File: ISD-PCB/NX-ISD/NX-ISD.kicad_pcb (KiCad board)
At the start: 4 copper layers, 77 x 45 mm, 79 parts, among them J1 1-2328702-0, P1 S2B-PH-SM4-TB, Q1 AO3400A, Q2 AO3401A, Q3 BC847W, Q4 AO3400A, U1 ESP32-S3-WROOM-1, U10 BNO085, U11 HYCW275-USBC24-050B, U12 OPT3001DNPR, U13 RT9193-18GB, U14 ZDSD02GLGEAG, U15 USBLC6-2P6, U2 NCP167BMX330TBG, U3 MAX17048G_T10, U4 RV-3028-C7, U5 MAX30102, U6 BME690, U7 TM-2025A, U8 BQ25170DSGR, U9 RT9193-28GB, Y2 32.768

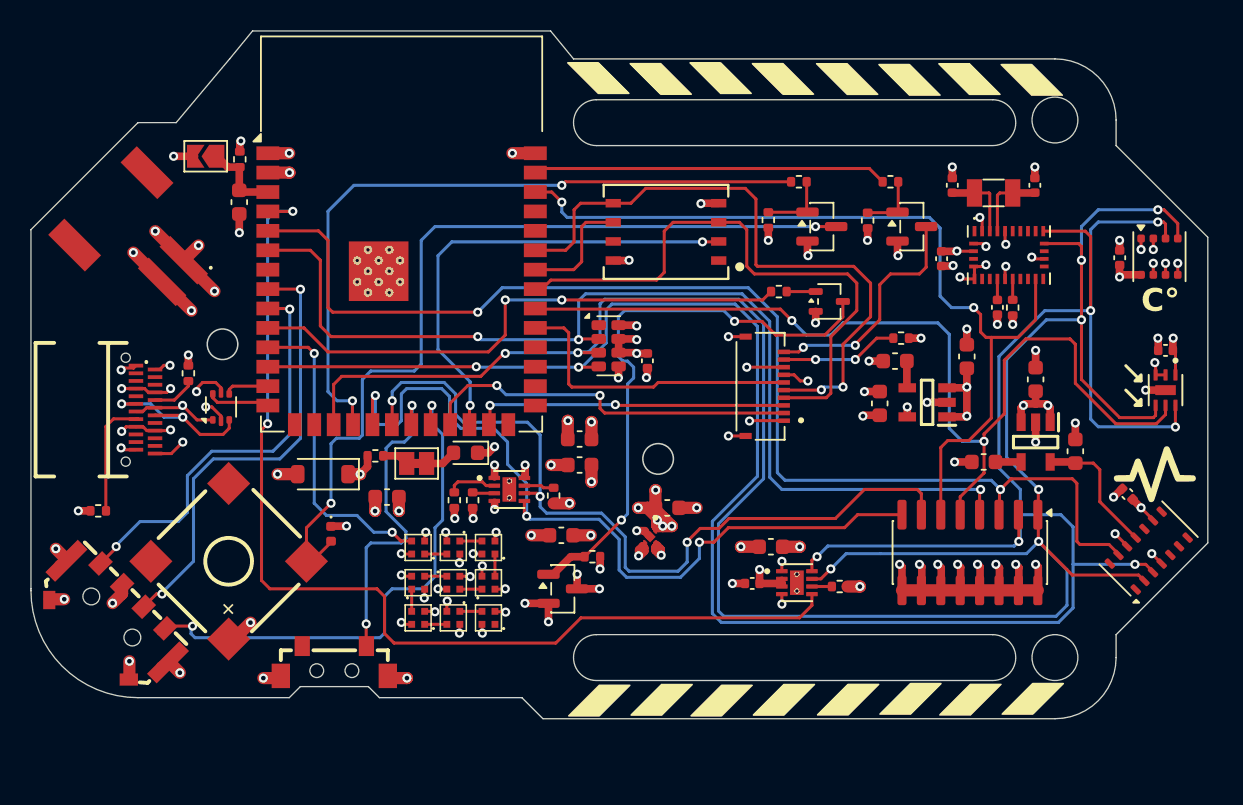
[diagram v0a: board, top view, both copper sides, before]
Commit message: Updated v1p0 files
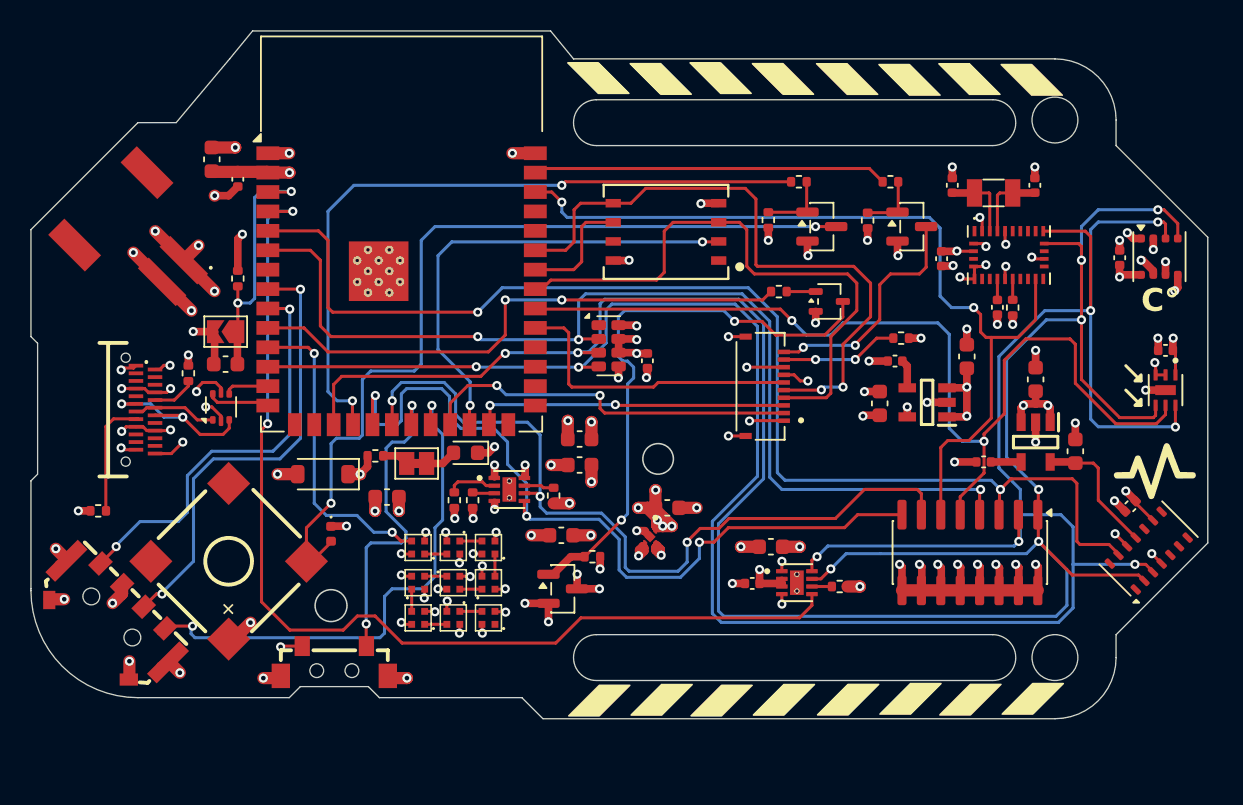
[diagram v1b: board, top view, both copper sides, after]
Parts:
- added C16: 10u, Capacitor_SMD:C_0603_1608Metric, F.Cu at (124.2, 86.5)
- added C17: 100n, Capacitor_SMD:C_0402_1005Metric, F.Cu at (125.9, 87.8)
- C11, C14: footprint Capacitor_SMD:C_0603_1608Metric -> Capacitor_SMD:C_0402_1005Metric
- C20, C21, C8: value 1uF -> 1u
- C22: value 10uF -> 10u
- S1: value TS18-5-15-SL-260 -> TS-1101VS-C-A-A
- moved JP2 11.5 mm to (125.1, 97.8)
- moved C8 10.6 mm to (125.1, 99.9), turned to 180 degrees
- moved R3 7.80 mm to (125.9, 94.3)
- moved C5 0.82 mm to (184.3, 109.2), turned to -135 degrees
- moved G*** 0.20 mm to (187.4, 106.9)
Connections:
- S1 pad 2: unconnected-(S1-Pad2) -> GND
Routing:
- net /Logic section/EN: track 5.25 -> 17.2 mm, vias 0 -> 2
- net GND: track 90.3 -> 97.5 mm, vias 86 -> 88
- net +3V3: track 63.1 -> 69.5 mm
- net /Power section/U_D+: track 5.78 -> 5.46 mm, vias 1 -> 0
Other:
- outline, holes or cut-outs redrawn
- board text added: "LED"
- board text added: "P: IO17 D: IO18"
- board text removed: "CHRG LED"
- board text removed: "POWER: IO17 DATA: IO18"

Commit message: updated label
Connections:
- net /Logic section/!INT_H renamed /Logic section/!INT_DOF
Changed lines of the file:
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@@
 			(layers "F.Cu" "F.Mask" "F.Paste")
 			(roundrect_rratio 0.25)
-			(net "/Logic section/!INT_H")
+			(net "/Logic section/!INT_DOF")
 			(pinfunction "R6.1_6")
 			(pintype "passive")
@@
 			(size 0.25 0.675)
 			(layers "F.Cu" "F.Mask" "F.Paste")
-			(net "/Logic section/!INT_H")
+			(net "/Logic section/!INT_DOF")
 			(pinfunction "~{H_INT}_14")
 			(pintype "output")
@@
 			(size 1.5 0.9)
 			(layers "F.Cu" "F.Mask" "F.Paste")
-			(net "/Logic section/!INT_H")
+			(net "/Logic section/!INT_DOF")
 			(pinfunction "IO2_38")
 			(pintype "bidirectional")
@@
 		(width 0.2)
 		(layer "F.Cu")
-		(net "/Logic section/!INT_H")
+		(net "/Logic section/!INT_DOF")
 	)
 	(segment
@@
 		(width 0.2)
 		(layer "F.Cu")
-		(net "/Logic section/!INT_H")
+		(net "/Logic section/!INT_DOF")
 	)
 	(segment
@@
 		(width 0.2)
 		(layer "F.Cu")
-		(net "/Logic section/!INT_H")
+		(net "/Logic section/!INT_DOF")
 	)
 	(segment
@@
 		(width 0.2)
 		(layer "F.Cu")
-		(net "/Logic section/!INT_H")
+		(net "/Logic section/!INT_DOF")
 	)
 	(segment
@@
 		(width 0.2)
 		(layer "F.Cu")
-		(net "/Logic section/!INT_H")
+		(net "/Logic section/!INT_DOF")
 	)
 	(segment
@@
 		(width 0.2)
 		(layer "F.Cu")
-		(net "/Logic section/!INT_H")
+		(net "/Logic section/!INT_DOF")
 	)
 	(segment
@@
 		(width 0.2)
 		(layer "F.Cu")
-		(net "/Logic section/!INT_H")
+		(net "/Logic section/!INT_DOF")
 	)
 	(segment
@@
 		(width 0.2)
 		(layer "F.Cu")
-		(net "/Logic section/!INT_H")
+		(net "/Logic section/!INT_DOF")
 	)
 	(segment
@@
 		(width 0.2)
 		(layer "F.Cu")
-		(net "/Logic section/!INT_H")
+		(net "/Logic section/!INT_DOF")
 	)
 	(segment
@@
 		(width 0.2)
 		(layer "F.Cu")
-		(net "/Logic section/!INT_H")
+		(net "/Logic section/!INT_DOF")
 	)
 	(segment
@@
 		(width 0.2)
 		(layer "F.Cu")
-		(net "/Logic section/!INT_H")
+		(net "/Logic section/!INT_DOF")
 	)
 	(segment
@@
 		(width 0.2)
 		(layer "F.Cu")
-		(net "/Logic section/!INT_H")
+		(net "/Logic section/!INT_DOF")
 	)
 	(segment
@@
 		(width 0.2)
 		(layer "F.Cu")
-		(net "/Logic section/!INT_H")
+		(net "/Logic section/!INT_DOF")
 	)
 	(segment
@@
 		(width 0.2)
 		(layer "F.Cu")
-		(net "/Logic section/!INT_H")
+		(net "/Logic section/!INT_DOF")
 	)
 	(via
@@
 		(drill 0.3)
 		(layers "F.Cu" "B.Cu")
-		(net "/Logic section/!INT_H")
+		(net "/Logic section/!INT_DOF")
 	)
 	(via
@@
 		(drill 0.3)
 		(layers "F.Cu" "B.Cu")
-		(net "/Logic section/!INT_H")
+		(net "/Logic section/!INT_DOF")
 	)
 	(segment
@@
 		(width 0.2)
 		(layer "B.Cu")
-		(net "/Logic section/!INT_H")
+		(net "/Logic section/!INT_DOF")
 	)
 	(segment
@@
 		(width 0.2)
 		(layer "B.Cu")
-		(net "/Logic section/!INT_H")
+		(net "/Logic section/!INT_DOF")
 	)
 	(segment
@@
 		(width 0.2)
 		(layer "B.Cu")
-		(net "/Logic section/!INT_H")
+		(net "/Logic section/!INT_DOF")
 	)
 	(segment
@@
 		(width 0.2)
 		(layer "B.Cu")
-		(net "/Logic section/!INT_H")
+		(net "/Logic section/!INT_DOF")
 	)
 	(segment
@@
 		(width 0.2)
 		(layer "B.Cu")
-		(net "/Logic section/!INT_H")
+		(net "/Logic section/!INT_DOF")
 	)
 	(segment
@@
 		(width 0.2)
 		(layer "B.Cu")
-		(net "/Logic section/!INT_H")
+		(net "/Logic section/!INT_DOF")
 	)
 	(segment
@@
 		(width 0.2)
 		(layer "B.Cu")
-		(net "/Logic section/!INT_H")
+		(net "/Logic section/!INT_DOF")
 	)
 	(segment

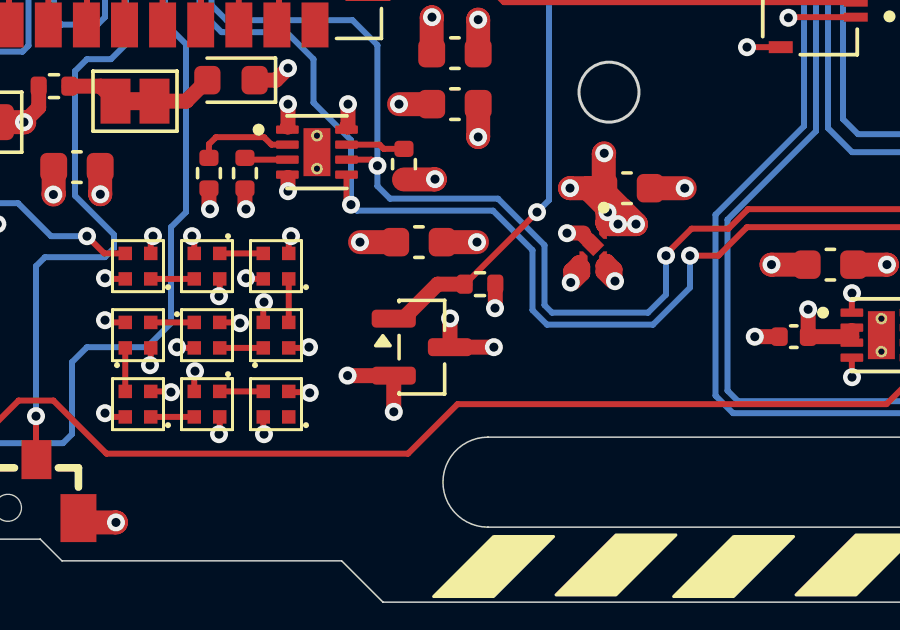
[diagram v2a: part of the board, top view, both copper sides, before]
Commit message: Fixed: polarity of NPM Pmos
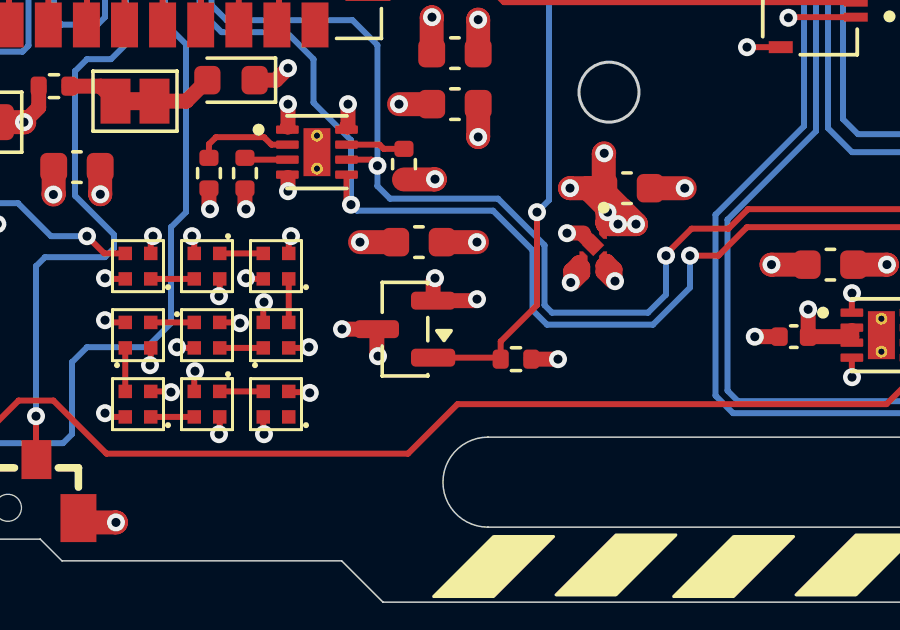
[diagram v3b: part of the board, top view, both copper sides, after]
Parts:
- moved R12 2.77 mm to (150.3, 115.0)
- moved Q2 0.82 mm to (146.6, 114.0), turned to 180 degrees
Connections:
- net /Logic section/!INT_DOF renamed /Logic section/!INT_H
- Q2 pad 2: VN -> VBAT
- Q2 pad 3: VBAT -> VN
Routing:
- net Net-(Q2-G): track 37.5 -> 38.9 mm
- net VN: track 8.44 -> 7.77 mm
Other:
- board text added: "v1p1"
- board text removed: "v1p0"

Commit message: v1p1 rework in progress
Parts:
- added C18: 100n, Capacitor_SMD:C_0402_1005Metric, F.Cu at (182.8, 112.1)
- added G10: XL-1010RGBC-WS2812B, NX-AW-footprints:LED-SMD_4P-L1.0-W1.0-TL_XL-1010RGBC-WS2812B, F.Cu at (139.6, 117.0)
- added G11: XL-1010RGBC-WS2812B, NX-AW-footprints:LED-SMD_4P-L1.0-W1.0-TL_XL-1010RGBC-WS2812B, F.Cu at (141.9, 117.0)
- added G12: XL-1010RGBC-WS2812B, NX-AW-footprints:LED-SMD_4P-L1.0-W1.0-TL_XL-1010RGBC-WS2812B, F.Cu at (144.1, 117.0)
- added G13: XL-1010RGBC-WS2812B, NX-AW-footprints:LED-SMD_4P-L1.0-W1.0-TL_XL-1010RGBC-WS2812B, F.Cu at (144.1, 119.3)
- added G14: XL-1010RGBC-WS2812B, NX-AW-footprints:LED-SMD_4P-L1.0-W1.0-TL_XL-1010RGBC-WS2812B, F.Cu at (141.9, 119.3)
- added G15: XL-1010RGBC-WS2812B, NX-AW-footprints:LED-SMD_4P-L1.0-W1.0-TL_XL-1010RGBC-WS2812B, F.Cu at (139.6, 119.3)
- added G16: XL-1010RGBC-WS2812B, NX-AW-footprints:LED-SMD_4P-L1.0-W1.0-TL_XL-1010RGBC-WS2812B, F.Cu at (137.2, 119.3)
- added JP3: BOOT, Jumper:SolderJumper-2_P1.3mm_Open_TrianglePad1.0x1.5mm, B.Cu at (135.8, 99.0)
- added R18: 10k, Resistor_SMD:R_0402_1005Metric, F.Cu at (171.5, 93.7)
- added R19: 10k, Resistor_SMD:R_0402_1005Metric, F.Cu at (180.1, 93.2)
- J1: footprint Global Footprints:TE_1-2328702-0 -> NX-AW-footprints:TE_1-2328702-0
- U14: footprint Global Footprints:LGA-8_L8.0-W6.0-P1.27-TL_ZDSD02GLGEAG -> NX-AW-footprints:LGA-8_L8.0-W6.0-P1.27-TL_ZDSD02GLGEAG
- moved G9 5.13 mm to (137.2, 117.1)
- moved R15 4.83 mm to (165.4, 101.0)
- moved G6 4.21 mm to (141.9, 114.8), turned to 0 degrees
- moved G5 4.14 mm to (144.1, 114.8), turned to 90 degrees
- moved R14 4.10 mm to (170.3, 88.0), turned to 0 degrees
- moved G8 3.23 mm to (137.3, 114.8), turned to 90 degrees
- moved G7 2.55 mm to (139.6, 114.8), turned to 90 degrees
- moved G4 2.49 mm to (144.1, 112.5), turned to 180 degrees
- moved S1 2.24 mm to (132.2, 121.6)
- moved U7 2.20 mm to (117.6, 118.7)
- moved RN1 2.06 mm to (173.8, 114.3)
- moved J1 1.91 mm to (162.9, 105.0)
- moved C1 1.51 mm to (183.4, 94.4)
- moved C12 1.51 mm to (186.4, 100.5)
- moved G*** 1.51 mm to (187.3, 108.4)
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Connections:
- net /Logic section/RS renamed /Logic section/DC
- net /Sernsor section/SCL_1 renamed /Logic section/SCL_1
- net /Sernsor section/SDA_1 renamed /Logic section/SDA_1
- G9 pad 1: unconnected-(G9-DOUT-Pad1) -> Net-(G10-DIN)
- U1 pad 27: unconnected-(U1-IO0-Pad27) -> /Logic section/BOOT
- U10 pad 18: unconnected-(U10-~{H_CS}-Pad18) -> Net-(U10-~{H_CS})
- U10 pad 4: unconnected-(U10-~{BOOT}-Pad4) -> Net-(U10-~{BOOT})
- U3 pad 10: GND -> (no net)
- U3 pad 11: GND -> (no net)
- U8 pad 10: GND -> (no net)
- U8 pad 11: GND -> (no net)
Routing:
- net /Logic section/SCL_1: track 155.4 -> 128.7 mm, vias 8 -> 7
- net /Logic section/SDA_1: track 166.2 -> 147.0 mm
- net /Logic section/!ALERT: track 68.4 -> 87.4 mm, vias 2 -> 3
- net GND: track 97.5 -> 80.0 mm, vias 88 -> 74
- net Net-(Q4-D): track 15.7 -> 0.00 mm, vias 2 -> 0
- net /Logic section/CS_TFT: track 20.8 -> 9.86 mm
- net /Logic section/BOOT: track 0.00 -> 10.3 mm, vias 0 -> 1
- net /Logic section/MOSI: track 41.4 -> 32.1 mm, vias 2 -> 0
- net /Logic section/SCK: track 38.6 -> 29.3 mm
- net /Logic section/!INT_HR: track 78.8 -> 70.5 mm
- net /Logic section/RST: track 19.9 -> 11.7 mm
- net Net-(J1-Pad9): track 7.82 -> 0.00 mm, vias 2 -> 0
- net +1V8: track 8.92 -> 3.33 mm
- net VN: track 7.77 -> 2.57 mm, vias 11 -> 3
- net /Logic section/LEVER_LEFT: track 34.5 -> 29.3 mm
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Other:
- board size 77 x 45 mm -> 77 x 48.6 mm

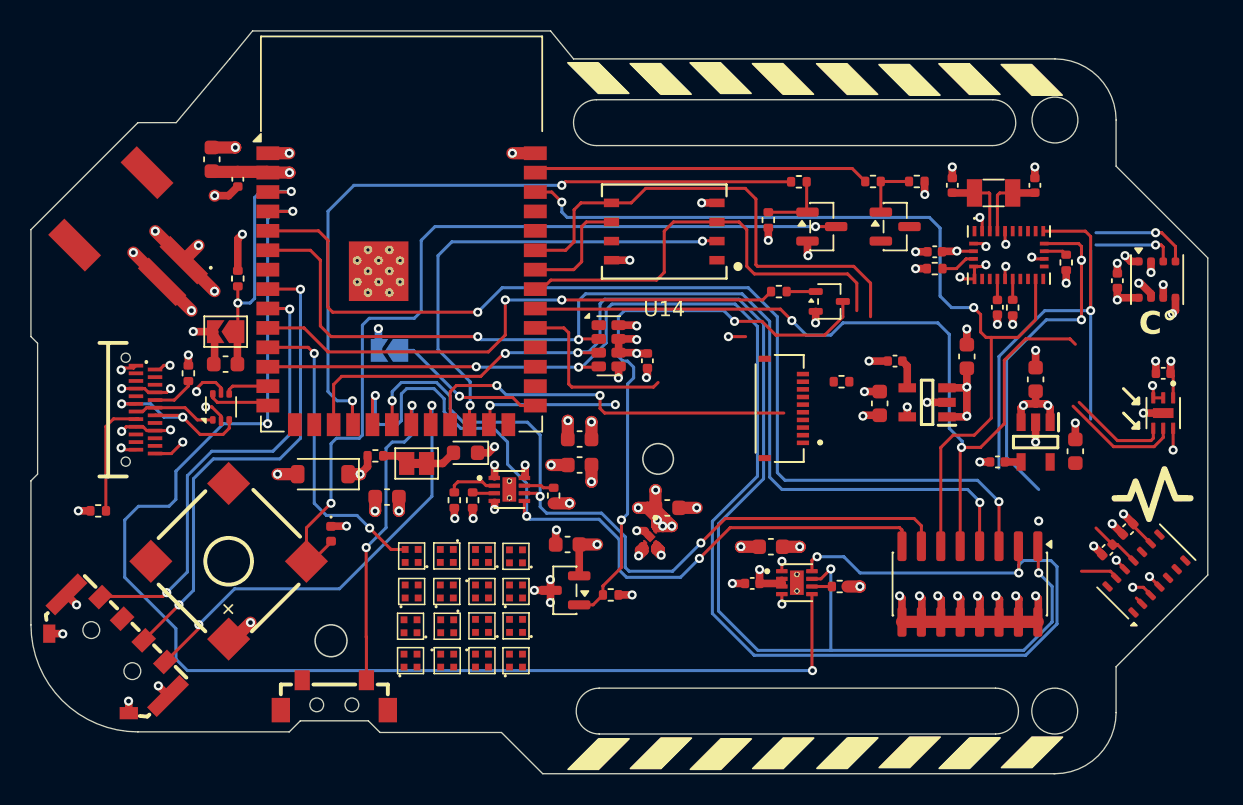
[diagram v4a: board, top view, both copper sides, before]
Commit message: added software planed feature and progress on v1p1
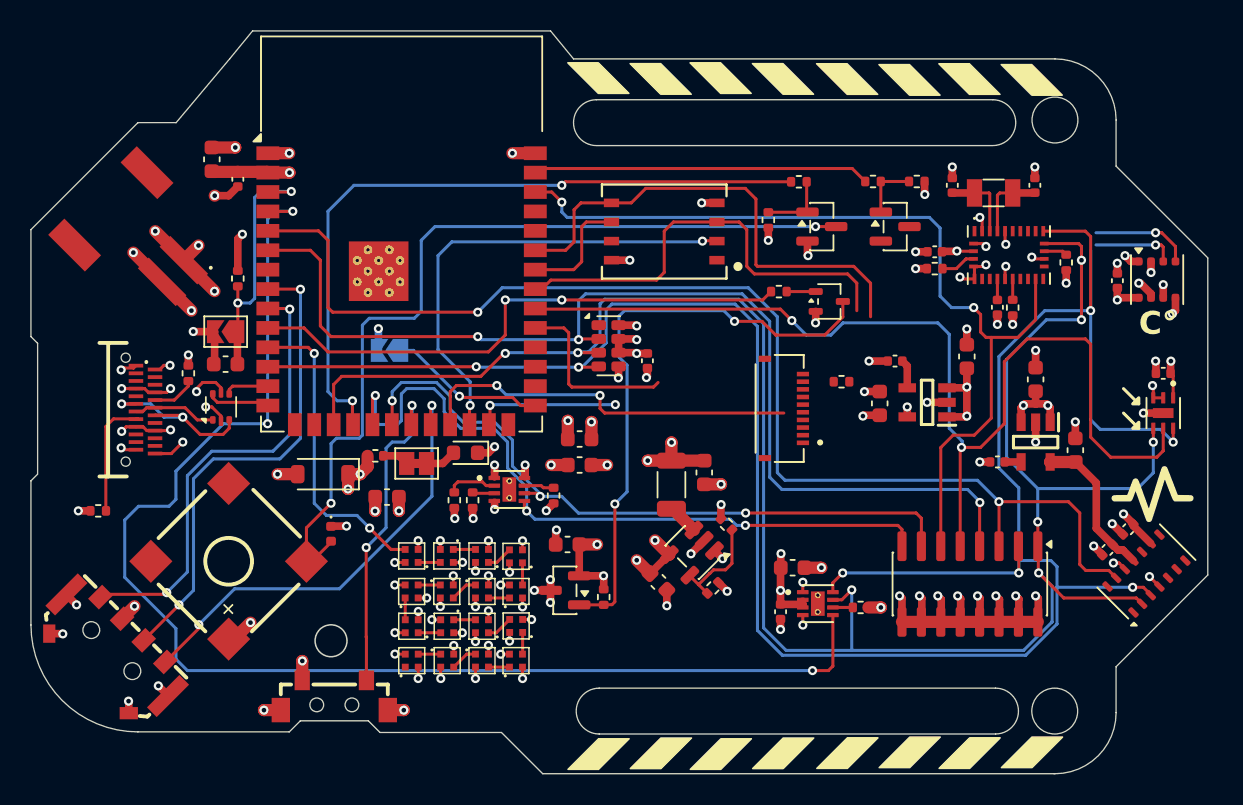
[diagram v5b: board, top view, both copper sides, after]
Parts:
- removed C3: 1u, Capacitor_SMD:C_0603_1608Metric
- added C19: 4.7u, Capacitor_SMD:C_0603_1608Metric, F.Cu at (153.4, 114.2)
- added C23: 10u, Capacitor_SMD:C_0603_1608Metric, F.Cu at (156.4, 107.0)
- added L1: 2.2u, Inductor_SMD:L_1206_3216Metric, F.Cu at (154.3, 107.8)
- added R16: 453k, Resistor_SMD:R_0402_1005Metric, F.Cu at (157.9, 110.4)
- added R20: 100k, Resistor_SMD:R_0402_1005Metric, F.Cu at (157.0, 114.5)
- D5: value D_Schottky_Filled -> NRVB230LSFT1G
- U2: value NCP167BMX330TBG -> TLV62568DBV; footprint Global Footprints:VREG_NCP167BMX330TBG -> Package_TO_SOT_SMD:SOT-23-5
- moved U2 2.92 mm to (155.6, 112.2), turned to -135 degrees
- moved C7 2.62 mm to (161.4, 116.1), turned to -90 degrees
- moved C4 1.97 mm to (162.2, 113.2)
- moved R6 1.94 mm to (166.7, 115.8)
- moved U3 1.94 mm to (163.8, 115.6)
- moved R12 0.48 mm to (149.8, 115.1), turned to 90 degrees
- moved G16 0.08 mm to (137.3, 119.3)
- moved G9 0.08 mm to (137.3, 117.1)
- moved C15 0.07 mm to (180.7, 105.5)
- turned G7 to 0 degrees
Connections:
- U2 pad 1: +3V3 -> VBAT
- U2 pad 3: VBAT -> Net-(U2-SW)
- U2 pad 5: GND -> Net-(U2-FB)
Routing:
- net GND: track 80.0 -> 94.8 mm, vias 74 -> 94
- net /Logic section/SDA_1: track 147.0 -> 159.0 mm
- net /Logic section/SCL_1: track 128.7 -> 138.9 mm, vias 7 -> 9
- net VN: track 2.57 -> 12.3 mm, vias 3 -> 19
- net /Logic section/!INT_HR: track 70.5 -> 79.7 mm
- net Net-(U2-FB): track 0.00 -> 6.63 mm
- net +1V8: track 3.33 -> 9.86 mm
- net /Logic section/!INT_ALS: track 63.5 -> 69.7 mm
- net /Logic section/USB_DETECT: track 50.7 -> 45.3 mm
- net VBAT: track 21.1 -> 25.8 mm, vias 12 -> 13
- net /Logic section/BAT_STAT: track 52.7 -> 48.3 mm
- net Net-(U2-SW): track 0.00 -> 2.05 mm
- net Net-(G6-DOUT): track 0.00 -> 1.80 mm
- net Net-(G14-DOUT): track 0.00 -> 1.78 mm
- net Net-(G11-DOUT): track 0.00 -> 1.75 mm
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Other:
- outline, holes or cut-outs redrawn

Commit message: v1p1 updates
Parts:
- L1: footprint Inductor_SMD:L_1206_3216Metric -> Inductor_SMD:L_1008_2520Metric
- RN1: value 8x4.7k -> YC248-JR-074K7L; footprint Package_SO:SOIC-16_3.9x9.9mm_P1.27mm -> NX-AW-footprints:RESCAXS50P400X160X55-16N
- moved J1 1.36 mm to (164.2, 105.2)
- moved RN1 1.27 mm to (172.6, 113.9)
- moved C23 0.63 mm to (156.9, 107.4)
- moved S1 0.51 mm to (132.2, 121.0)
- moved L1 0.13 mm to (154.4, 107.8)
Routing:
- net /Logic section/SCL_1: track 138.9 -> 153.3 mm
- net +3V3: track 69.3 -> 55.0 mm, vias 32 -> 28
- net /Logic section/BAT_STAT: track 48.3 -> 50.9 mm
- net /Logic section/USB_DETECT: track 45.3 -> 47.3 mm
- net Net-(U2-SW): track 2.05 -> 0.08 mm
- net /Logic section/!INT_HR: track 79.7 -> 81.6 mm
- net /Logic section/SCK: track 29.3 -> 27.7 mm
- net /Logic section/!INT_ALS: track 69.7 -> 71.2 mm
- net /Logic section/SDA_1: track 159.0 -> 157.7 mm, vias 8 -> 9
- net /Logic section/BTN: track 21.0 -> 22.3 mm
- net /Logic section/!INT_H: track 59.3 -> 60.6 mm
- net /Logic section/!INT_RTC: track 70.2 -> 70.9 mm
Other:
- outline, holes or cut-outs redrawn
